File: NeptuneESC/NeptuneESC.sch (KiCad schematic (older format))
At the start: 19 parts, among them U3 ATmega8A-AU, Y2 16MHz

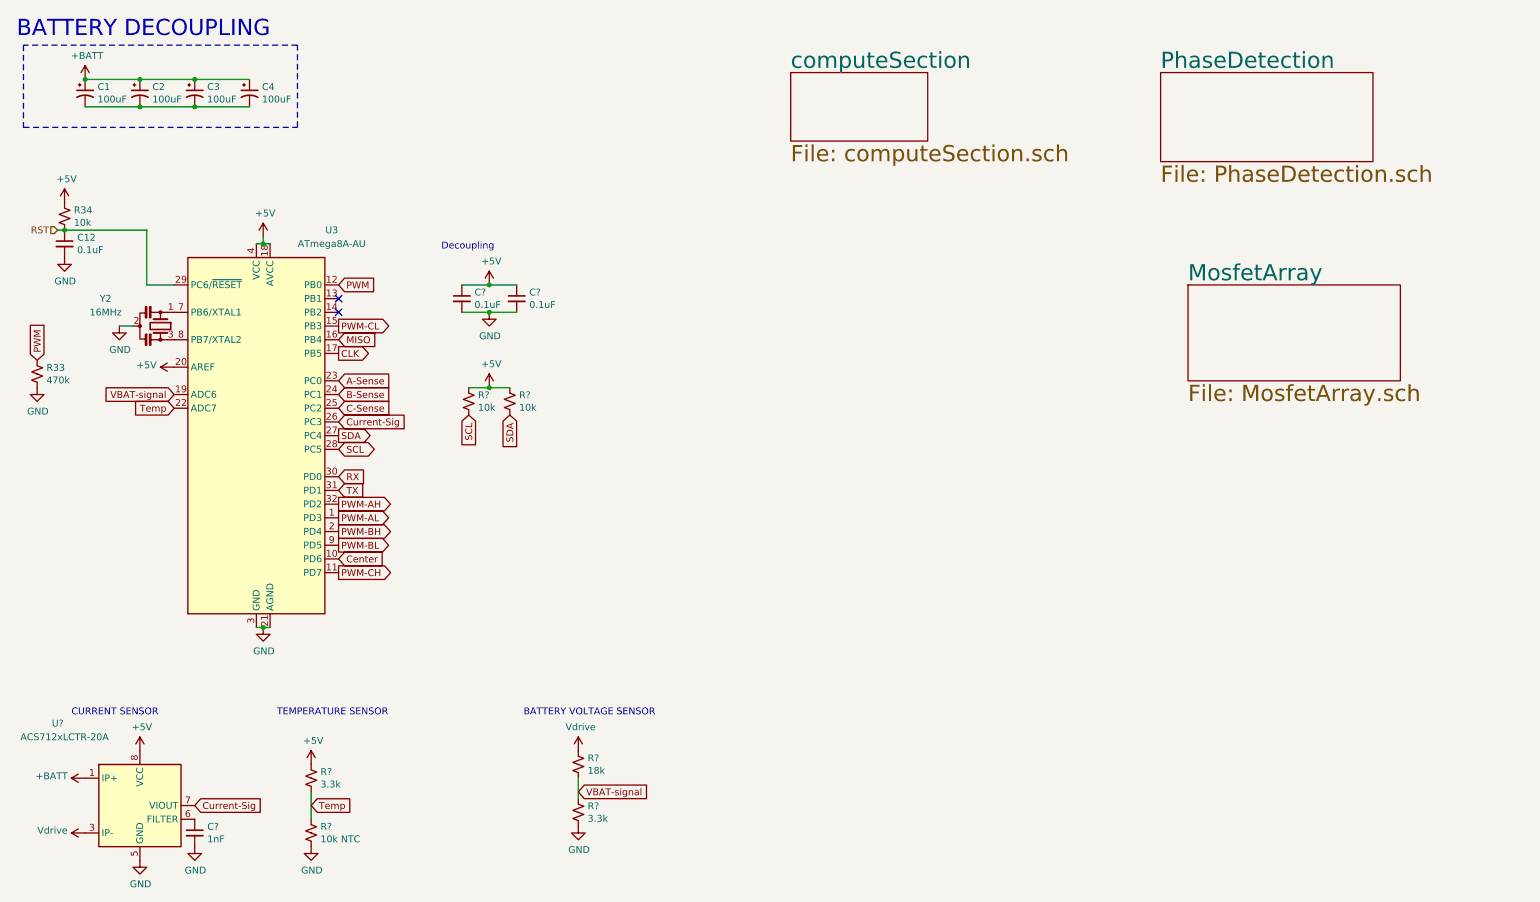
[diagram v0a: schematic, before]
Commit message: Innitial layout
Need to add motor pads
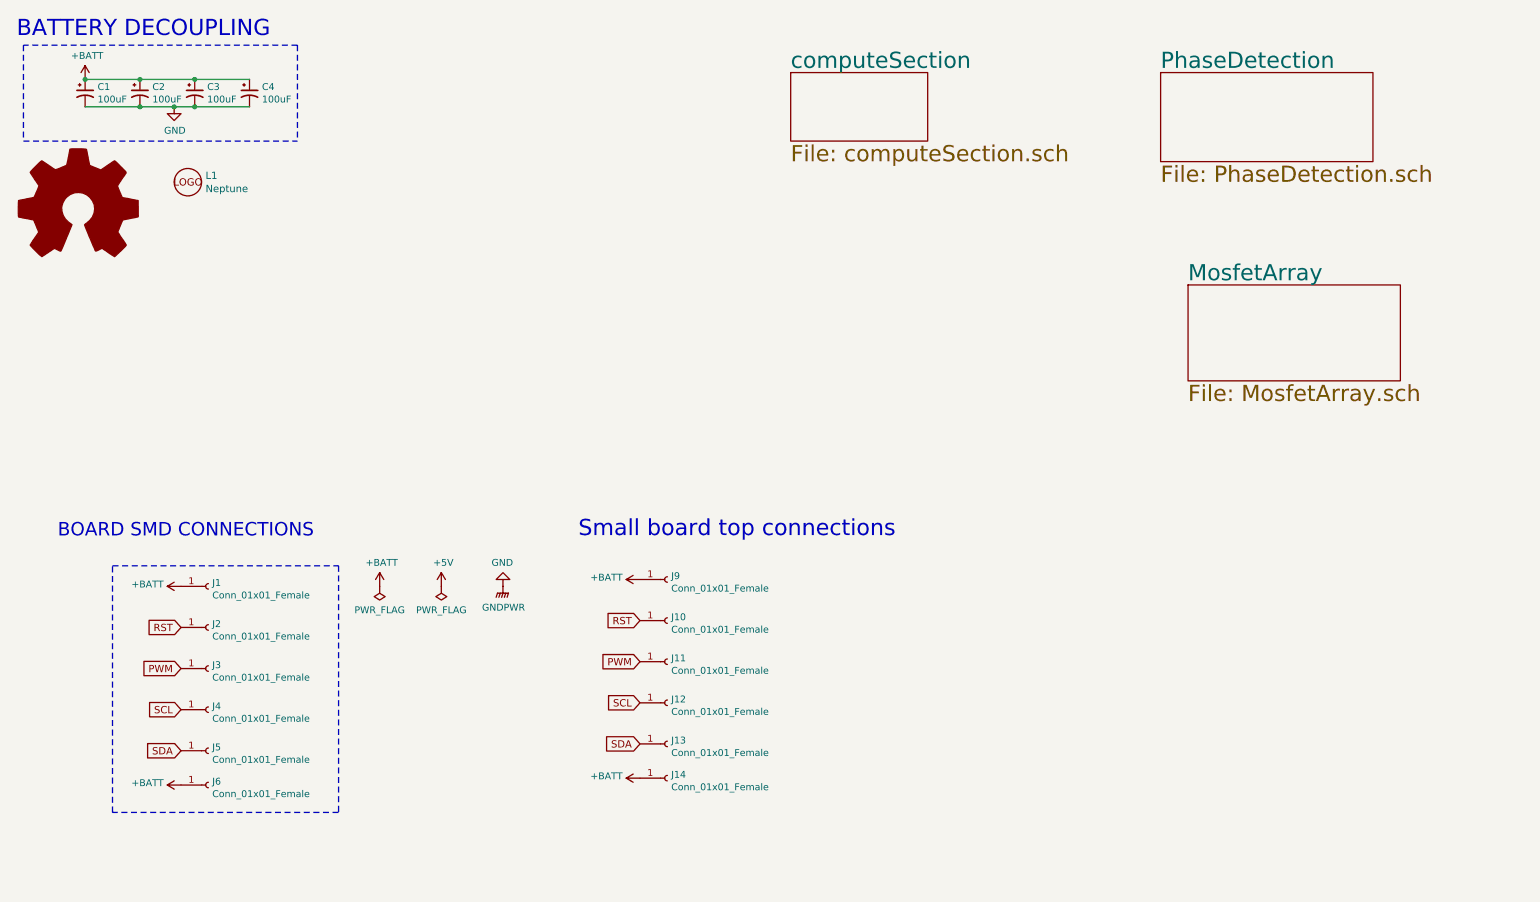
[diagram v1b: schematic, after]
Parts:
- removed C12, C? (x2): 0.1uF, symbol Device:C_Small
- removed C?: 1nF, symbol Device:C_Small
- removed R33: 470k, symbol Device:R_Small_US
- removed R34, R? (x2): 10k, symbol Device:R_Small_US
- removed R?: 10k NTC, symbol Device:R_Small_US
- removed R? (x2): 3.3k, symbol Device:R_Small_US
- removed R?: 18k, symbol Device:R_Small_US
- removed U3: ATmega8A-AU, Package_QFP:TQFP-32_7x7mm_P0.8mm, symbol MCU_Microchip_ATmega:ATmega8A-AU
- removed U?: ACS712xLCTR-20A, Package_SO:SOIC-8_3.9x4.9mm_P1.27mm, symbol Sensor_Current:ACS712xLCTR-20A
- removed Y2: 16MHz, symbol Device:Resonator_Small
- added J1, J2, J3, J4, J5, J6: Conn_01x01_Female, TestPoint:TestPoint_Pad_4.0x4.0mm, symbol Connector:Conn_01x01_Female
- added J10, J11, J12, J13, J14, J9: Conn_01x01_Female, TestPoint:TestPoint_Pad_1.0x1.0mm, symbol Connector:Conn_01x01_Female
- added L1: Neptune, Logos:neptuneLogo, symbol SS8050-G:Neptune
- C1, C2, C3, C4: footprint (none) -> Capacitor_Tantalum_SMD:CP_EIA-7343-43_Kemet-X
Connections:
- net +BATT: now also J1.1 (Pin_1), J14.1 (Pin_1), J6.1 (Pin_1), J9.1 (Pin_1)
- net GND: now also C1.2, C2.2, C3.2, C4.2
- net PWM: now also J11.1 (Pin_1), J3.1 (Pin_1)
- net RST: now also J10.1 (Pin_1), J2.1 (Pin_1)
- net SCL: now also J12.1 (Pin_1), J4.1 (Pin_1)
- net SDA: now also J13.1 (Pin_1), J5.1 (Pin_1)
- no-connect marks 2 -> 0
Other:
- note added: "BOARD SMD CONNECTIONS\n"
- note added: "Small board top connections\n"
- note removed: "BATTERY VOLTAGE SENSOR"
- note removed: "CURRENT SENSOR\n"
- note removed: "Decoupling"
- note removed: "TEMPERATURE SENSOR"
